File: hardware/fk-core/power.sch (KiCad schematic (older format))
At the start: 39 parts, among them CN1 DCBARRELSMT, CN2 JST_2PIN-SMT, P1 USB_OTG, U2 MCP73871, U3 INA219, U4 INA219, U6 TPS63060, U7 MAX1704XX

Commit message: Adding some connectors to get to various power lines.
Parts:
- added P3, P4: CONN_01X02, symbol CONN_01X02
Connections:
- wire segments 158 -> 217

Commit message: Adding GPS connector and BOM placeholder.
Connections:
- wire segments 217 -> 165

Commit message: Assigning most of the footprints.
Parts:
- C11, C12, C13, C14, C15, C16, C17, C18, C19, C8, C9: footprint (none) -> Capacitors_SMD:C_0805_HandSoldering
- C4, C5, C6, C7: footprint (none) -> Capacitors_SMD:CP_Elec_5x4.5
- CN2: footprint JST-PH-2-SMT -> Connectors_JST:JST_PH_B2B-PH-SM4-TB_02x2.00mm_Straight
- L1: footprint (none) -> Inductors:Inductor_Wurth_MAPI-3020
- P1: footprint (none) -> Connectors:USB_Micro-B
- P3, P4: footprint (none) -> Socket_Strips:Socket_Strip_Straight_1x02
- R10, R11: footprint (none) -> Resistors_SMD:R_2512_HandSoldering
- R12, R13, R14, R15, R16, R17, R3, R4, R5, R6, R7, R8, R9: footprint (none) -> Resistors_SMD:R_0805_HandSoldering
- U2: footprint (none) -> Housings_DFN_QFN:QFN-20-1EP_4x4mm_Pitch0.5mm
- U3, U4: footprint (none) -> SMD_Packages:SOIC-8-N
- U6: footprint (none) -> WSON-10:WSON-10-2x3
- U7: footprint (none) -> Housings_DFN_QFN:DFN-8-1EP_3x2mm_Pitch0.5mm

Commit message: Better footprints, swapping GPS for FGPMMOPA6H
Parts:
- CN1: footprint DCJACK_2MM_SMT -> CUI-PJ-002AH-SMT_dc-barrel-jack:CUI-PJ-002AH-SMT_dc-barrel-jack
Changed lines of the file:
@@
 LIBS:max1704xx
 LIBS:gp-635tsmd
+LIBS:fgpmmopa6h
 LIBS:fk-core-cache
 EELAYER 25 0
@@
 F 0 "CN1" H 7050 5500 45  0000 L BNN
 F 1 "DCBARRELSMT" H 7050 5100 45  0000 L BNN
-F 2 "DCJACK_2MM_SMT" H 7280 5450 20  0001 C CNN
+F 2 "CUI-PJ-002AH-SMT_dc-barrel-jack:CUI-PJ-002AH-SMT_dc-barrel-jack" H 7280 5450 20  0001 C CNN
 F 3 "" H 7250 5300 60  0001 C CNN
 F 4 "CP-002AHPJCT-ND" H 7250 5300 60  0001 C CNN "SPN"

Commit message: Adding a neopixel, maybe gonna use it. Also some more jumpers.
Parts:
- added P6, P7: CONN_01X02, Socket_Strips:Socket_Strip_Straight_1x02, symbol CONN_01X02
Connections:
- wire segments 165 -> 169

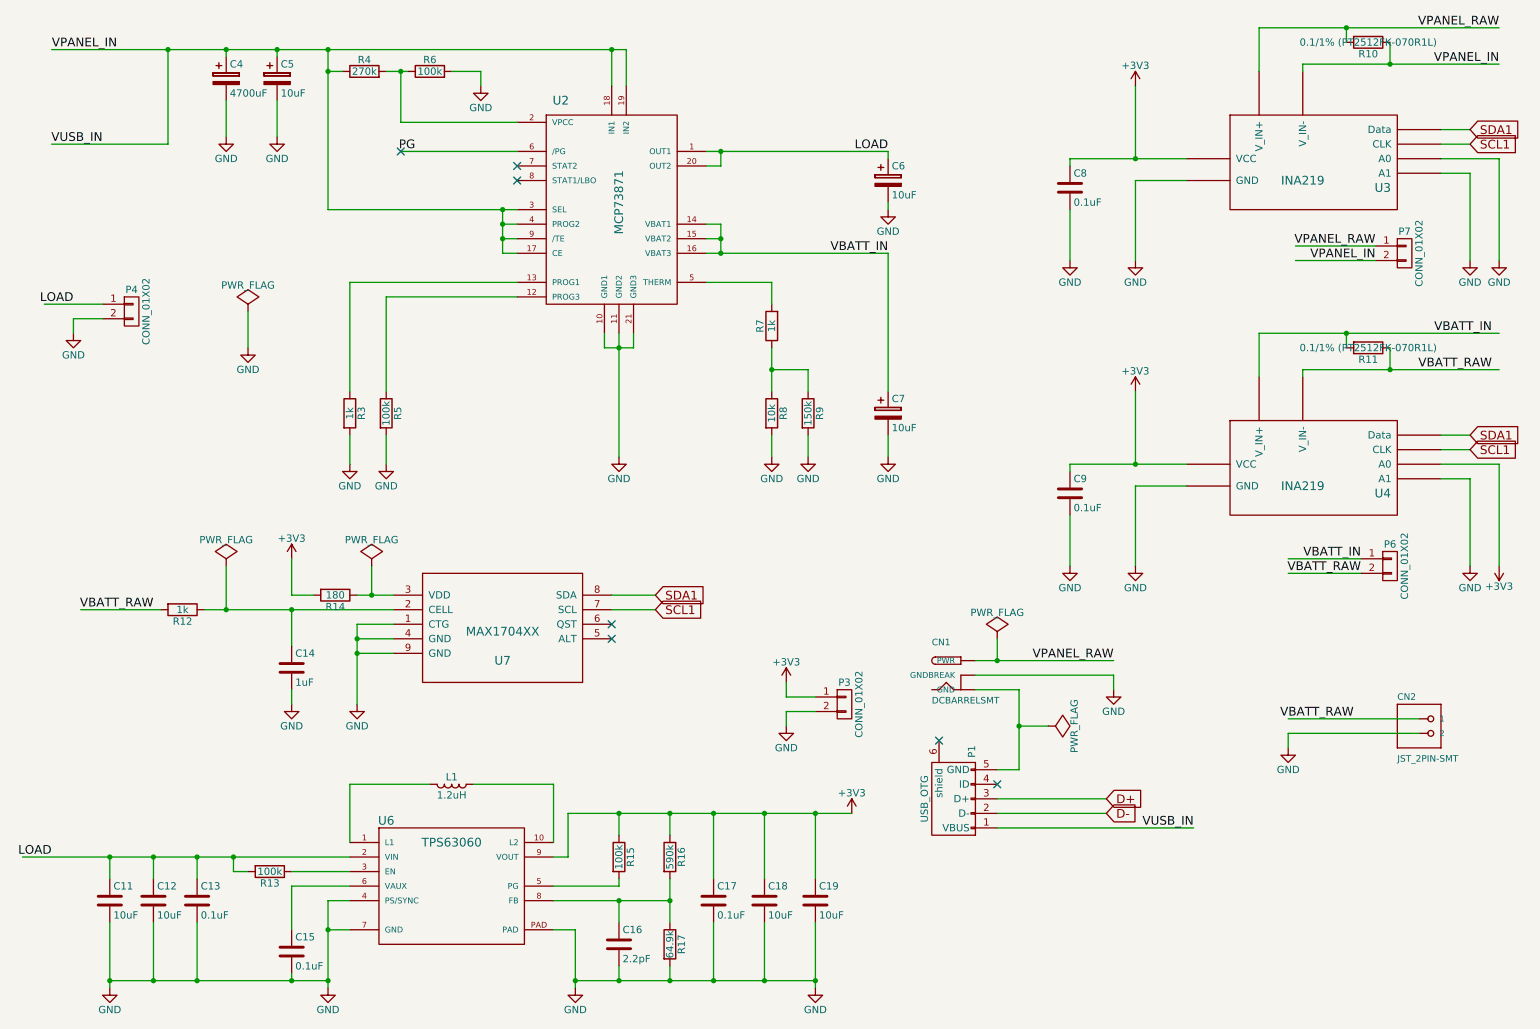
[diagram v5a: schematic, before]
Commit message: Tweaking positions.
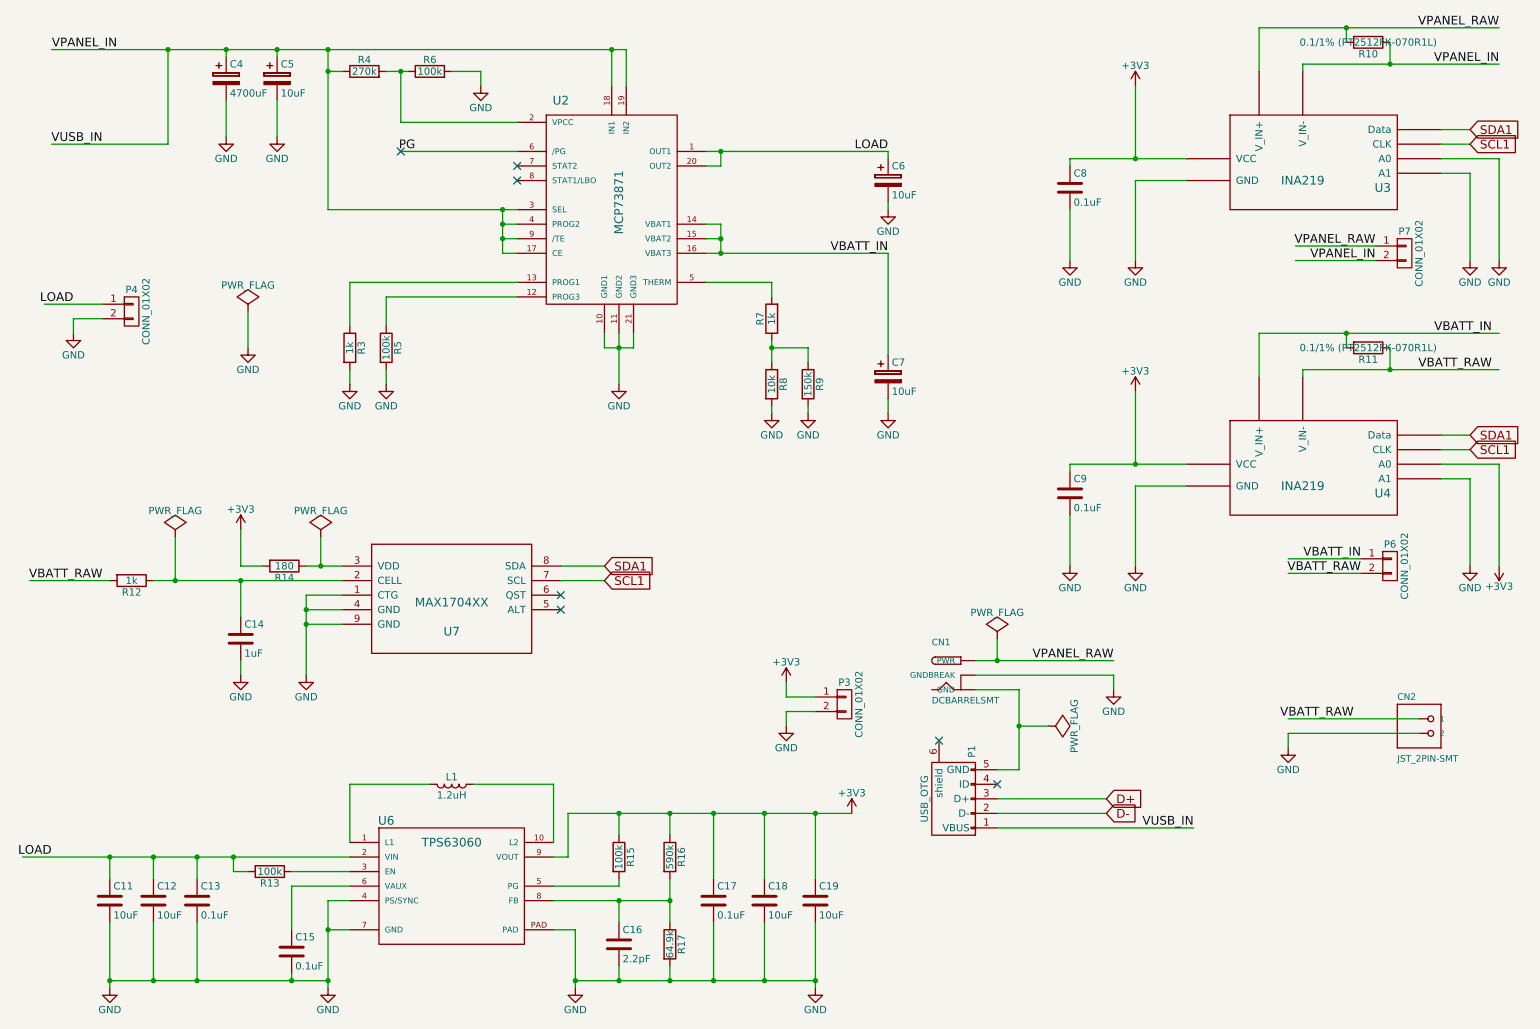
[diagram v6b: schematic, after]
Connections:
- wire segments 169 -> 221
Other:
- moved on the sheet: C14, C7, R12, R14, R3, R5, R7, R8, R9, U7

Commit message: Cleaning up footprints and libraries.
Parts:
- CN1: SPN CP-002AHPJCT-ND -> (none)
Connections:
- wire segments 221 -> 169
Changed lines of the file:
@@
 LIBS:microsd
 LIBS:pcf8523t
-LIBS:xtal32x15
 LIBS:tps63060
 LIBS:max1704xx
@@
 LIBS:fgpmmopa6h
 LIBS:sk6812
+LIBS:dcbarrelsmt
+LIBS:xtal-3.2x1
 LIBS:fk-core-cache
 EELAYER 25 0
@@
 	8450 1900 8450 2450
 Wire Wire Line
-	8000 1750 8450 1750
-Wire Wire Line
-	8450 1750 8800 1750
+	8000 1750 8800 1750
 Wire Wire Line
 	8450 1750 8450 1250
@@
 	8800 4000 8450 4000
 Wire Wire Line
-	8000 3850 8450 3850
-Wire Wire Line
-	8450 3850 8800 3850
+	8000 3850 8800 3850
 Wire Wire Line
 	8450 3850 8450 3350
@@
 	6750 1700 6750 1750
 Wire Wire Line
-	5500 1700 5600 1700
-Wire Wire Line
-	5600 1700 6750 1700
+	5500 1700 6750 1700
 Wire Wire Line
 	5500 1800 5600 1800
@@
 	6200 3500 6200 3450
 Wire Wire Line
-	5950 3000 5950 3050
-Wire Wire Line
-	5950 3050 5950 3150
+	5950 3000 5950 3150
 Wire Wire Line
 	6200 3150 6200 3050
@@
 Connection ~ 5950 3050
 Wire Wire Line
-	5500 2400 5600 2400
-Wire Wire Line
-	5600 2400 6750 2400
-Wire Wire Line
-	5600 2200 5600 2300
-Wire Wire Line
-	5600 2300 5600 2400
+	5500 2400 6750 2400
+Wire Wire Line
+	5600 2200 5600 2400
 Wire Wire Line
 	5600 2200 5500 2200
@@
 Connection ~ 5600 2400
 Wire Wire Line
-	4900 2950 4900 3050
-Wire Wire Line
-	4900 3050 4900 3300
+	4900 2950 4900 3300
 Wire Wire Line
 	5000 3050 5000 2950
 Wire Wire Line
-	4800 3050 4900 3050
-Wire Wire Line
-	4900 3050 5000 3050
+	4800 3050 5000 3050
 Connection ~ 4900 3050
 Wire Wire Line
@@
 	3050 2600 4200 2600
 Wire Wire Line
-	3300 1150 3400 1150
-Wire Wire Line
-	3400 1150 3450 1150
+	3300 1150 3450 1150
 Wire Wire Line
 	4200 1500 3400 1500
@@
 	3950 1150 3750 1150
 Wire Wire Line
-	2900 2100 4100 2100
-Wire Wire Line
-	4100 2100 4200 2100
-Wire Wire Line
-	4100 2100 4100 2200
-Wire Wire Line
-	4100 2200 4100 2300
-Wire Wire Line
-	4100 2300 4100 2400
+	2900 2100 4200 2100
+Wire Wire Line
+	4100 2100 4100 2400
 Wire Wire Line
 	4100 2200 4200 2200
@@
 	2900 1150 3000 1150
 Wire Wire Line
-	2900 1000 2900 1150
-Wire Wire Line
-	2900 1150 2900 2100
+	2900 1000 2900 2100
 Connection ~ 2900 1000
 Connection ~ 2900 1150
 Wire Wire Line
-	1000 1000 1800 1000
-Wire Wire Line
-	1800 1000 2200 1000
-Wire Wire Line
-	2200 1000 2550 1000
-Wire Wire Line
-	2550 1000 2900 1000
-Wire Wire Line
-	2900 1000 4850 1000
-Wire Wire Line
-	4850 1000 4950 1000
+	1000 1000 4950 1000
 Wire Wire Line
 	1800 1650 1800 1000
@@
 Connection ~ 1800 1000
 Wire Wire Line
-	9600 3200 10200 3200
-Wire Wire Line
-	10200 3200 10950 3200
+	9600 3200 10950 3200
 Wire Wire Line
 	9600 3200 9600 3250
@@
 	9600 1150 9600 1100
 Wire Wire Line
-	9600 1100 10200 1100
-Wire Wire Line
-	10200 1100 10950 1100
+	9600 1100 10950 1100
 Wire Wire Line
 	9300 1150 9300 850
 Wire Wire Line
-	9300 850  9900 850
-Wire Wire Line
-	9900 850  10950 850
+	9300 850  10950 850
 Wire Wire Line
 	9900 950  9900 850
@@
 Connection ~ 10200 1100
 Wire Wire Line
-	9300 2950 9900 2950
-Wire Wire Line
-	9900 2950 10950 2950
+	9300 2950 10950 2950
 Text Label 6750 1700 2    60   ~ 0
 LOAD
@@
 	0    -1   -1   0
 $EndComp
-$Comp
-L DCBARRELSMT CN1
-U 1 1 5880AA9C
-P 7250 5300
-F 0 "CN1" H 7050 5500 45  0000 L BNN
-F 1 "DCBARRELSMT" H 7050 5100 45  0000 L BNN
-F 2 "CUI-PJ-002AH-SMT_dc-barrel-jack:CUI-PJ-002AH-SMT_dc-barrel-jack" H 7280 5450 20  0001 C CNN
-F 3 "" H 7250 5300 60  0001 C CNN
-F 4 "CP-002AHPJCT-ND" H 7250 5300 60  0001 C CNN "SPN"
-	1    7250 5300
-	1    0    0    -1
-$EndComp
 Wire Wire Line
 	7500 6150 8250 6150
@@
 	7350 5400 7650 5400
 Wire Wire Line
-	7650 5400 7650 5650
-Wire Wire Line
-	7650 5650 7650 5950
+	7650 5400 7650 5950
 Wire Wire Line
 	7650 5950 7500 5950
@@
 $EndComp
 Wire Wire Line
-	7350 5200 7500 5200
-Wire Wire Line
-	7500 5200 8300 5200
+	7350 5200 8300 5200
 Text Label 8300 5200 2    60   ~ 0
 VPANEL_RAW
@@
 	4450 7050 4600 7050
 Wire Wire Line
-	4600 7050 4600 7400
-Wire Wire Line
-	4600 7400 4600 7450
+	4600 7050 4600 7450
 Wire Wire Line
 	3050 7050 2900 7050
 Wire Wire Line
-	2900 6850 2900 7050
-Wire Wire Line
-	2900 7050 2900 7400
-Wire Wire Line
-	2900 7400 2900 7450
+	2900 6850 2900 7450
 $Comp
 L R R13
@@
 	3050 6650 2650 6650
 Wire Wire Line
-	800  6550 1400 6550
-Wire Wire Line
-	1400 6550 1700 6550
-Wire Wire Line
-	1700 6550 2000 6550
-Wire Wire Line
-	2000 6550 2250 6550
-Wire Wire Line
-	2250 6550 3050 6550
+	800  6550 3050 6550
 $Comp
 L C C13
@@
 Connection ~ 1700 6550
 Wire Wire Line
-	1400 7000 1400 7400
-Wire Wire Line
-	1400 7400 1400 7450
+	1400 7000 1400 7450
 Connection ~ 1700 7400
 Wire Wire Line
@@
 Connection ~ 2000 7400
 Wire Wire Line
-	1400 7400 1700 7400
-Wire Wire Line
-	1700 7400 2000 7400
-Wire Wire Line
-	2000 7400 2650 7400
-Wire Wire Line
-	2650 7400 2900 7400
+	1400 7400 2900 7400
 $Comp
 L C C16
@@
 	4900 7000 4900 6850
 Wire Wire Line
-	4450 6850 4900 6850
-Wire Wire Line
-	4900 6850 5250 6850
-Wire Wire Line
-	5250 6700 5250 6850
-Wire Wire Line
-	5250 6850 5250 7000
+	4450 6850 5250 6850
+Wire Wire Line
+	5250 6700 5250 7000
 Connection ~ 4900 6850
 Connection ~ 5250 6850
@@
 $EndComp
 Wire Wire Line
-	6250 7000 6250 7400
-Wire Wire Line
-	6250 7400 6250 7450
+	6250 7000 6250 7450
 Connection ~ 6250 7400
 Wire Wire Line
@@
 Connection ~ 6250 6250
 Wire Wire Line
-	4550 6250 4900 6250
-Wire Wire Line
-	4900 6250 5250 6250
-Wire Wire Line
-	5250 6250 5550 6250
-Wire Wire Line
-	5550 6250 5900 6250
-Wire Wire Line
-	5900 6250 6250 6250
-Wire Wire Line
-	6250 6250 6500 6250
-Wire Wire Line
-	4600 7400 4900 7400
-Wire Wire Line
-	4900 7400 5250 7400
-Wire Wire Line
-	5250 7400 5550 7400
-Wire Wire Line
-	5550 7400 5900 7400
-Wire Wire Line
-	5900 7400 6250 7400
+	4550 6250 6500 6250
+Wire Wire Line
+	4600 7400 6250 7400
 Wire Wire Line
 	5900 7000 5900 7400
@@
 	2750 4850 3000 4850
 Wire Wire Line
-	2750 4750 2750 4850
-Wire Wire Line
-	2750 4850 2750 4950
-Wire Wire Line
-	2750 4950 2750 5300
+	2750 4750 2750 5300
 Wire Wire Line
 	2750 4950 3000 4950
@@
 $EndComp
 Wire Wire Line
-	2750 4550 2850 4550
-Wire Wire Line
-	2850 4550 3000 4550
-Wire Wire Line
-	1700 4650 1850 4650
-Wire Wire Line
-	1850 4650 2300 4650
-Wire Wire Line
-	2300 4650 3000 4650
+	2750 4550 3000 4550
+Wire Wire Line
+	1700 4650 3000 4650
 $Comp
 L PWR_FLAG #FLG049
@@
 Wire Wire Line
 	9500 4600 10000 4600
+$Comp
+L DCBARRELSMT CN1
+U 1 1 5880D794
+P 7250 5300
+F 0 "CN1" H 7050 5500 45  0000 L BNN
+F 1 "DCBARRELSMT" H 7050 5100 45  0000 L BNN
+F 2 "CUI-PJ-002AH-SMT_dc-barrel-jack:CUI-PJ-002AH-SMT_dc-barrel-jack" H 7280 5450 20  0001 C CNN
+F 3 "" H 7250 5300 60  0001 C CNN
+	1    7250 5300
+	1    0    0    -1
+$EndComp
 $EndSCHEMATC
